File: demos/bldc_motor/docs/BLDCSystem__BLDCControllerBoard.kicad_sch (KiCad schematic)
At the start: 10 parts, among them J1 Header1xNFemale, J2 Header1xNFemale, J3 Header1xNFemale

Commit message: framework: passive + diode terminals mandatory (#30)
Continuation of the LED.cathode regression fix (#29). Resistor,
Capacitor, Inductor, and every Diode subclass had their terminals
declared `mandatory=False` with the same "structurally inert under
graph evaluation" justification — letting demos declare BOM-only
timing / decoupling / pull-up parts without wiring them, then ship
breadboard SVGs and netlists where those parts sat orphaned.

A real resistor / capacitor / inductor / diode with a dangling
terminal does nothing. Marking the ports mandatory closes the
silent regression at the framework layer.

  - `src/components/passives/{resistor,capacitor,inductor}.py` and
    every diode subclass under `src/components/diodes/` now declare
    their terminals `mandatory=True`.
  - `tests/components/test_{resistor,capacitor,inductor}.py`:
    regression tests pin the new contract per component.
  - `tests/components/test_diode_mandatory_terminals.py` (new):
    parametrized over D1N4001 / D1N4007 / D1N4148 / D1N4728A /
    D1N4733A / D1N4742A / D1N5817.
  - Six demos (`backup_power`, `bldc_motor`, `dice`,
    `doorbell_protector`, `fan_cooling`, `isolated_rs232`) had
    declared-but-unwired passives — each now wires them either to
    their datasheet-correct net (e.g. DoorbellProtector's flyback
    diode anode joins the relay coil_minus net) or as an isolated
    0-Ω passthrough with `dynamically_driven=True` where the part
    is genuinely BOM-only and the voltage-only simulator can't
    honour its behaviour. Comments at each call site explain
    which kind.
  - Test fixtures across CLI, refdes, format-roundtrip, kicad
    import, and per-format renderer tests updated so they still
    pin down the specific error each one exists to catch without
    tripping the new mandatory-pin check first.
  - All demo docs regenerated; goldens refreshed.

After this commit the breadboard SVGs show every BOM part connected
to something — no more orphaned caps and resistors float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
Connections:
- net Net-(C2-t1): now reaches C2.1
- net Net-(C2-t1): now also C2.2
- net Net-(C3-t1): now reaches C3.1
- net Net-(C3-t1): now also C3.2
- net Net-(R1-t1): now reaches R1.1
- net Net-(R1-t1): now also R1.2
- net Net-(C4-t1): now reaches C4.1
- net Net-(C4-t1): now also C4.2
- net Net-(C1-t1): now reaches C1.1
- net Net-(C1-t1): now also C1.2
- net Net-(C5-t1): now reaches C5.1
- net Net-(C5-t1): now also C5.2
- net Net-(C6-t1): now reaches C6.1
- net Net-(C6-t1): now also C6.2
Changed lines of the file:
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@@
     (stroke (width 0) (type default))
+  )
+  (global_label "Net-(C1-t1)"
+    (shape input)
+    (at 63.5 31.75 0)
+    (fields_autoplaced yes)
+    (effects (font (size 1.27 1.27)) (justify right))
+    (property "Intersheet References" "${INTERSHEET_REFS}"
+      (at 0 0 0)
+      (effects (font (size 1.27 1.27)) (hide yes))
+    )
   )
   (wire
     (pts (xy 63.5 21.59) (xy 63.5 19.05))
     (stroke (width 0) (type default))
+  )
+  (global_label "Net-(C1-t1)"
+    (shape input)
+    (at 63.5 19.05 0)
+    (fields_autoplaced yes)
+    (effects (font (size 1.27 1.27)) (justify right))
+    (property "Intersheet References" "${INTERSHEET_REFS}"
+      (at 0 0 0)
+      (effects (font (size 1.27 1.27)) (hide yes))
+    )
   )
   (symbol
@@
     (stroke (width 0) (type default))
   )
+  (global_label "Net-(C2-t1)"
+    (shape input)
+    (at 63.5 69.85 0)
+    (fields_autoplaced yes)
+    (effects (font (size 1.27 1.27)) (justify right))
+    (property "Intersheet References" "${INTERSHEET_REFS}"
+      (at 0 0 0)
+      (effects (font (size 1.27 1.27)) (hide yes))
+    )
+  )
   (wire
     (pts (xy 63.5 59.69) (xy 63.5 57.15))
     (stroke (width 0) (type default))
+  )
+  (global_label "Net-(C2-t1)"
+    (shape input)
+    (at 63.5 57.15 0)
+    (fields_autoplaced yes)
+    (effects (font (size 1.27 1.27)) (justify right))
+    (property "Intersheet References" "${INTERSHEET_REFS}"
+      (at 0 0 0)
+      (effects (font (size 1.27 1.27)) (hide yes))
+    )
   )
   (symbol
@@
     (stroke (width 0) (type default))
   )
+  (global_label "Net-(C3-t1)"
+    (shape input)
+    (at 63.5 107.95 0)
+    (fields_autoplaced yes)
+    (effects (font (size 1.27 1.27)) (justify right))
+    (property "Intersheet References" "${INTERSHEET_REFS}"
+      (at 0 0 0)
+      (effects (font (size 1.27 1.27)) (hide yes))
+    )
+  )
   (wire
     (pts (xy 63.5 97.79) (xy 63.5 95.25))
     (stroke (width 0) (type default))
+  )
+  (global_label "Net-(C3-t1)"
+    (shape input)
+    (at 63.5 95.25 0)
+    (fields_autoplaced yes)
+    (effects (font (size 1.27 1.27)) (justify right))
+    (property "Intersheet References" "${INTERSHEET_REFS}"
+      (at 0 0 0)
+      (effects (font (size 1.27 1.27)) (hide yes))
+    )
   )
   (symbol
@@
     (stroke (width 0) (type default))
   )
+  (global_label "Net-(C4-t1)"
+    (shape input)
+    (at 63.5 146.05 0)
+    (fields_autoplaced yes)
+    (effects (font (size 1.27 1.27)) (justify right))
+    (property "Intersheet References" "${INTERSHEET_REFS}"
+      (at 0 0 0)
+      (effects (font (size 1.27 1.27)) (hide yes))
+    )
+  )
   (wire
     (pts (xy 63.5 135.89) (xy 63.5 133.35))
     (stroke (width 0) (type default))
+  )
+  (global_label "Net-(C4-t1)"
+    (shape input)
+    (at 63.5 133.35 0)
+    (fields_autoplaced yes)
+    (effects (font (size 1.27 1.27)) (justify right))
+    (property "Intersheet References" "${INTERSHEET_REFS}"
+      (at 0 0 0)
+      (effects (font (size 1.27 1.27)) (hide yes))
+    )
   )
   (symbol
@@
     (stroke (width 0) (type default))
   )
+  (global_label "Net-(C5-t1)"
+    (shape input)
+    (at 63.5 184.15 0)
+    (fields_autoplaced yes)
+    (effects (font (size 1.27 1.27)) (justify right))
+    (property "Intersheet References" "${INTERSHEET_REFS}"
+      (at 0 0 0)
+      (effects (font (size 1.27 1.27)) (hide yes))
+    )
+  )
   (wire
     (pts (xy 63.5 173.99) (xy 63.5 171.45))
     (stroke (width 0) (type default))
+  )
+  (global_label "Net-(C5-t1)"
+    (shape input)
+    (at 63.5 171.45 0)
+    (fields_autoplaced yes)
+    (effects (font (size 1.27 1.27)) (justify right))
+    (property "Intersheet References" "${INTERSHEET_REFS}"
+      (at 0 0 0)
+      (effects (font (size 1.27 1.27)) (hide yes))
+    )
   )
   (symbol
@@
     (stroke (width 0) (type default))
   )
+  (global_label "Net-(C6-t1)"
+    (shape input)
+    (at 63.5 222.25 0)
+    (fields_autoplaced yes)
+    (effects (font (size 1.27 1.27)) (justify right))
+    (property "Intersheet References" "${INTERSHEET_REFS}"
+      (at 0 0 0)
+      (effects (font (size 1.27 1.27)) (hide yes))
+    )
+  )
   (wire
     (pts (xy 63.5 212.09) (xy 63.5 209.55))
     (stroke (width 0) (type default))
+  )
+  (global_label "Net-(C6-t1)"
+    (shape input)
+    (at 63.5 209.55 0)
+    (fields_autoplaced yes)
+    (effects (font (size 1.27 1.27)) (justify right))
+    (property "Intersheet References" "${INTERSHEET_REFS}"
+      (at 0 0 0)
+      (effects (font (size 1.27 1.27)) (hide yes))
+    )
   )
   (symbol
@@
     (stroke (width 0) (type default))
   )
+  (global_label "Net-(R1-t1)"
+    (shape input)
+    (at 63.5 565.15 0)
+    (fields_autoplaced yes)
+    (effects (font (size 1.27 1.27)) (justify right))
+    (property "Intersheet References" "${INTERSHEET_REFS}"
+      (at 0 0 0)
+      (effects (font (size 1.27 1.27)) (hide yes))
+    )
+  )
   (wire
     (pts (xy 63.5 554.99) (xy 63.5 552.45))
     (stroke (width 0) (type default))
+  )
+  (global_label "Net-(R1-t1)"
+    (shape input)
+    (at 63.5 552.45 0)
+    (fields_autoplaced yes)
+    (effects (font (size 1.27 1.27)) (justify right))
+    (property "Intersheet References" "${INTERSHEET_REFS}"
+      (at 0 0 0)
+      (effects (font (size 1.27 1.27)) (hide yes))
+    )
   )
   (symbol
@@
     (stroke (width 0) (type default))
   )
+  (wire
+    (pts (xy 63.5 19.05) (xy 63.5 31.75))
+    (stroke (width 0) (type default))
+  )
+  (wire
+    (pts (xy 63.5 57.15) (xy 63.5 69.85))
+    (stroke (width 0) (type default))
+  )
+  (wire
+    (pts (xy 63.5 95.25) (xy 63.5 107.95))
+    (stroke (width 0) (type default))
+  )
+  (wire
+    (pts (xy 63.5 133.35) (xy 63.5 146.05))
+    (stroke (width 0) (type default))
+  )
+  (wire
+    (pts (xy 63.5 171.45) (xy 63.5 184.15))
+    (stroke (width 0) (type default))
+  )
+  (wire
+    (pts (xy 63.5 209.55) (xy 63.5 222.25))
+    (stroke (width 0) (type default))
+  )
+  (wire
+    (pts (xy 63.5 552.45) (xy 63.5 565.15))
+    (stroke (width 0) (type default))
+  )

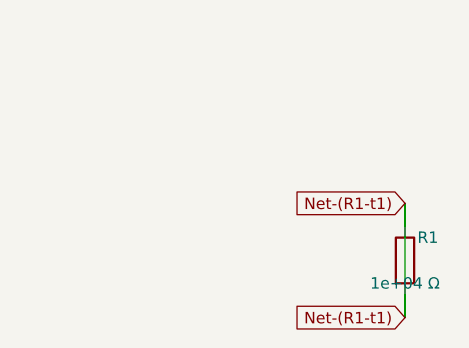
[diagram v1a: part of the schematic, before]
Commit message: units: Ohms.__str__ uses engineering notation (kΩ, MΩ, GΩ)
The previous `Ohms.__str__` formatted with bare `:.3g`, producing
unreadable scientific output for clean kilo / mega multiples:

  str(Ohms(10_000))     == "1e+04 Ω"      → now "10 kΩ"
  str(Ohms(100_000))    == "1e+05 Ω"      → now "100 kΩ"
  str(Ohms(1_000_000))  == "1e+06 Ω"      → now "1 MΩ"

The breadboard SVG visualiser surfaced the problem: a resistor body
labelled "100000Ω" makes a reader count zeros, while a label of
"100 kΩ" reads at a glance — exactly the convention every schematic
and parts catalogue uses. Centralising the engineering notation in
`Ohms.__str__` means every downstream consumer (assembly guide,
breadboard SVG, kicad netlist, BOM, reports) inherits the readable
form without each format adapter rolling its own formatter.

  - `Ohms.__str__` returns "47 Ω", "4.7 kΩ", "10 kΩ", "100 kΩ",
    "1 MΩ", "10 MΩ", "1 GΩ" per the kilo / mega / giga thresholds.
  - `Resistor.__str__` delegates to `str(self._ohms)` so it
    inherits the new notation (was producing the noisy "47.0 Ω"
    via raw float).
  - The breadboard visualiser's resistor body label uses
    `str(part.ohms)` directly (previously had a private
    `_format_ohms_compact` helper; removed).
  - `tests/components/test_resistor.py::test_str` updated for
    "47 Ω" (was "47.0 Ω"); new `test_str_renders_in_engineering_notation`
    pins kΩ / MΩ output across the kilo and mega thresholds.
  - All demo docs / goldens refreshed where the Ohms.__str__
    change affected the rendered output (breadboard SVGs, kicad
    sch value fields, BOM rows).
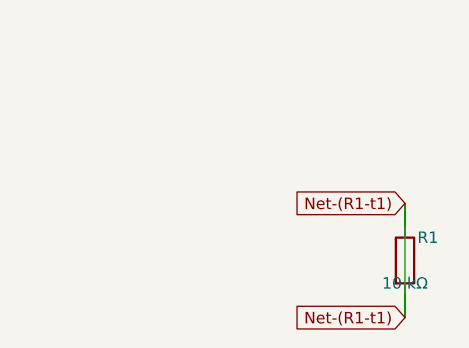
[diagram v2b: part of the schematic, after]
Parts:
- R1: value 1e+04 Ω -> 10 kΩ
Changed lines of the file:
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@@
       (effects (font (size 1.27 1.27)))
     )
-    (property "Value" "1e+04 Ω"
+    (property "Value" "10 kΩ"
       (at 63.5 561.34 0)
       (effects (font (size 1.27 1.27)))

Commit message: units: Farads + Henries __str__ also use engineering notation
Same treatment as `Ohms.__str__` (previous commit) for the other two
passive engineering quantities. Demos contain caps and inductors
with values that the bare `:.3g` formatter would emit in scientific
form (`1e-07 F` for a 100 nF decoupling cap); centralising the
engineering notation on the unit class means every consumer
(reports, BOM, breadboard SVG, etc.) inherits the readable form.

  - `Farads.__str__` returns `100 pF`, `22 nF`, `100 nF`, `1 µF`,
    `4.7 µF`, `470 µF`, `1 mF`, `1 F` across the standard
    capacitance bands.
  - `Henries.__str__` returns `100 nH`, `10 µH`, `22 mH`, `1 H`
    across the standard inductance bands.
  - `Capacitor.__str__` and `Inductor.__str__` delegate to the
    unit class's str (were rolling raw-float formatters).
  - `framework.export.reports_common.part_description` now uses
    `str(part.ohms / farads / henries)` directly instead of the
    parallel `_format_ohms` / `_format_farads` / `_format_henries`
    helpers (removed — they duplicated the new logic on raw
    floats).
  - Breadboard SVG renderer now also labels capacitor and inductor
    bodies with their engineering-notation value (was only
    resistors).
  - `tests/framework/test_units.py`: parametrised regression tests
    for both unit classes across every band.
  - All affected demo docs / goldens refreshed.
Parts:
- C1, C2, C3, C4: value 1e-08 F -> 10 nF
- C5: value 1e-07 F -> 100 nF
- C6: value 1e-05 F -> 10 µF
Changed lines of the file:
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@@
       (effects (font (size 1.27 1.27)))
     )
-    (property "Value" "1e-08 F"
+    (property "Value" "10 nF"
       (at 63.5 27.94 0)
       (effects (font (size 1.27 1.27)))
@@
       (effects (font (size 1.27 1.27)))
     )
-    (property "Value" "1e-08 F"
+    (property "Value" "10 nF"
       (at 63.5 66.04 0)
       (effects (font (size 1.27 1.27)))
@@
       (effects (font (size 1.27 1.27)))
     )
-    (property "Value" "1e-08 F"
+    (property "Value" "10 nF"
       (at 63.5 104.14 0)
       (effects (font (size 1.27 1.27)))
@@
       (effects (font (size 1.27 1.27)))
     )
-    (property "Value" "1e-08 F"
+    (property "Value" "10 nF"
       (at 63.5 142.24 0)
       (effects (font (size 1.27 1.27)))
@@
       (effects (font (size 1.27 1.27)))
     )
-    (property "Value" "1e-07 F"
+    (property "Value" "100 nF"
       (at 63.5 180.34 0)
       (effects (font (size 1.27 1.27)))
@@
       (effects (font (size 1.27 1.27)))
     )
-    (property "Value" "1e-05 F"
+    (property "Value" "10 µF"
       (at 63.5 218.44 0)
       (effects (font (size 1.27 1.27)))
